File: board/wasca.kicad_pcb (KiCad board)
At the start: 2 copper layers, 64 parts, among them CN1 CARTRIDGE_EDGE_CONNECTOR, CON1 SD_Card, CON2 USB_OTG, CON3 Thermal_Quad, IC1 MT48LC32M16A2TG, U1 74ALVC164245, U2 74ALVC164245, U3 74ALVC164245, U4 74ALVC164245, U5 LD1117S33CTR, U6 10M04SFE144C8G, U7 FT201XS

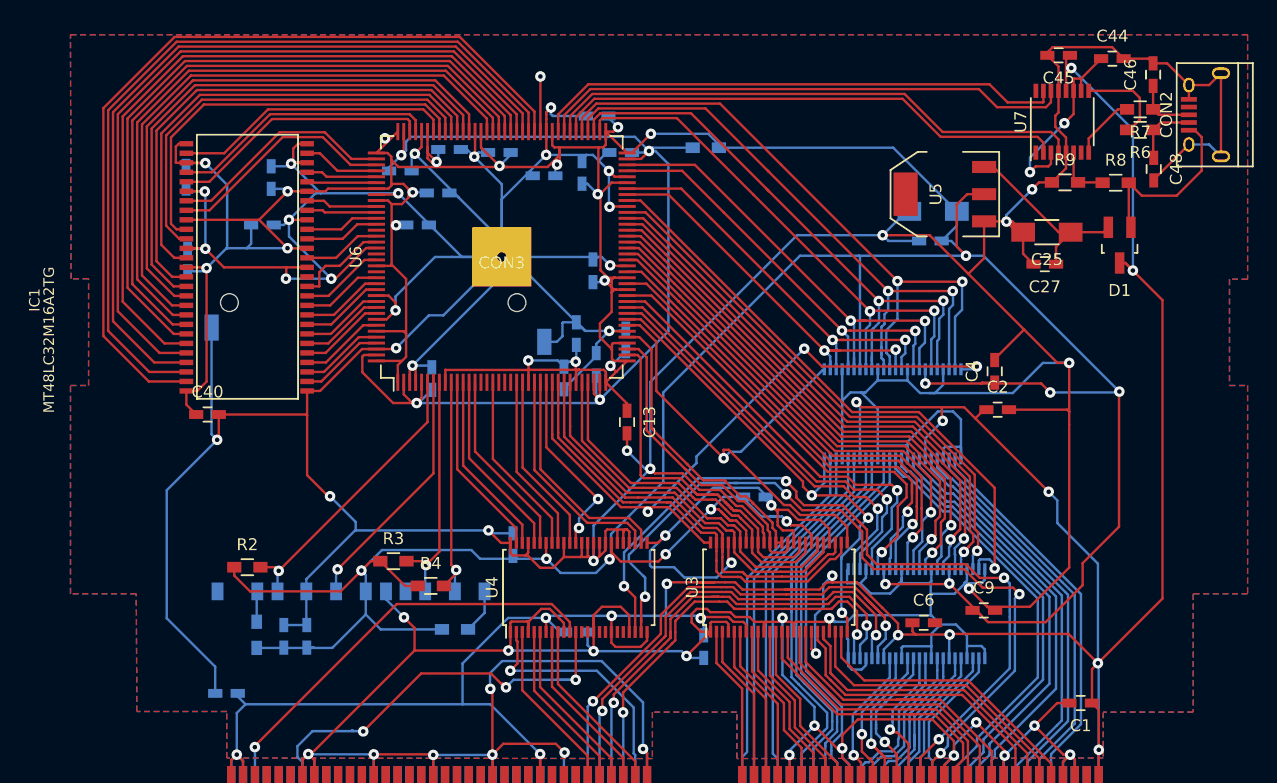
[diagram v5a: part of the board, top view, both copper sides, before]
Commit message: Silkscreen fix
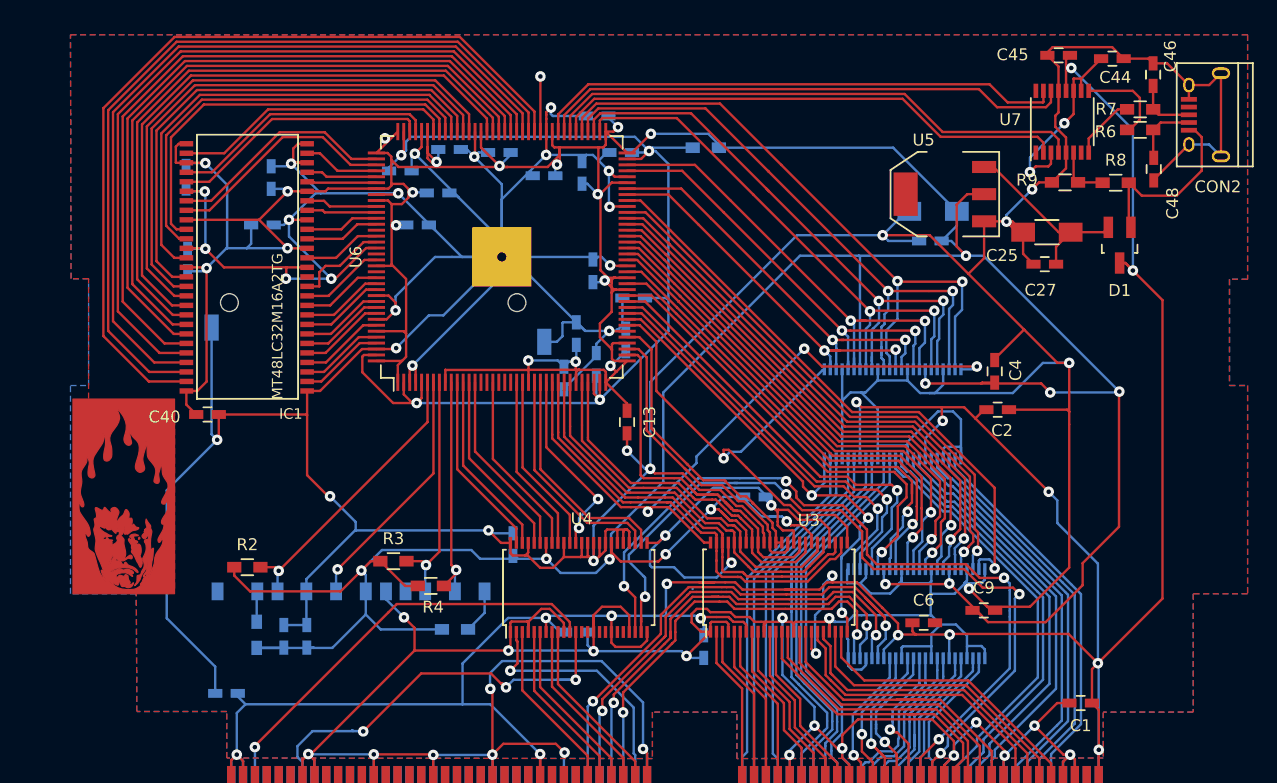
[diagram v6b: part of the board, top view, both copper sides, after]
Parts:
- added G***: LOGO, Wasca:Segata_Sanshiro, F.Cu at (31.8, 127.6)
- moved C28 18.3 mm to (74.7, 110.9), turned to 180 degrees
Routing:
- net /+3_3V: track 485.3 -> 487.6 mm
- net GND: track 972.5 -> 973.8 mm

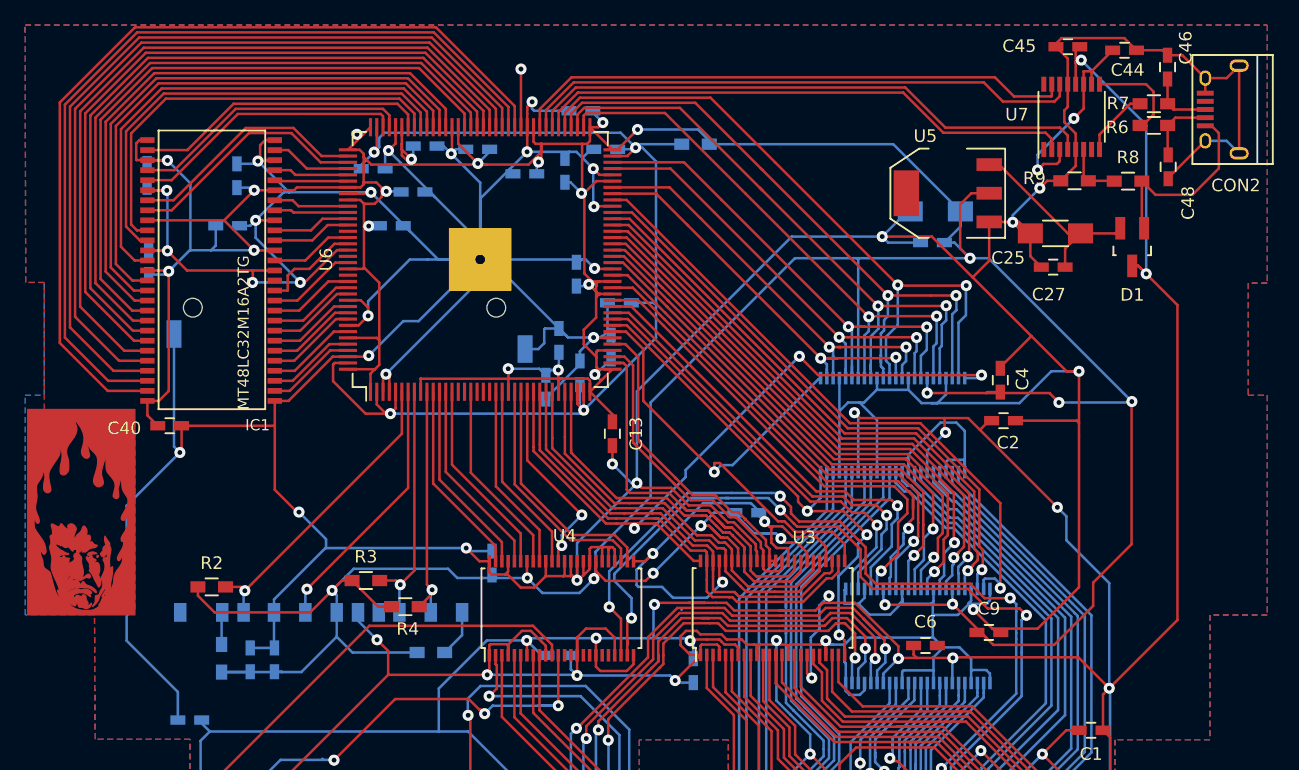
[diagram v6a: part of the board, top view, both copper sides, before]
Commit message: Board cleanup, intersected parts fix (thanks cafealpha2), more ground vias.
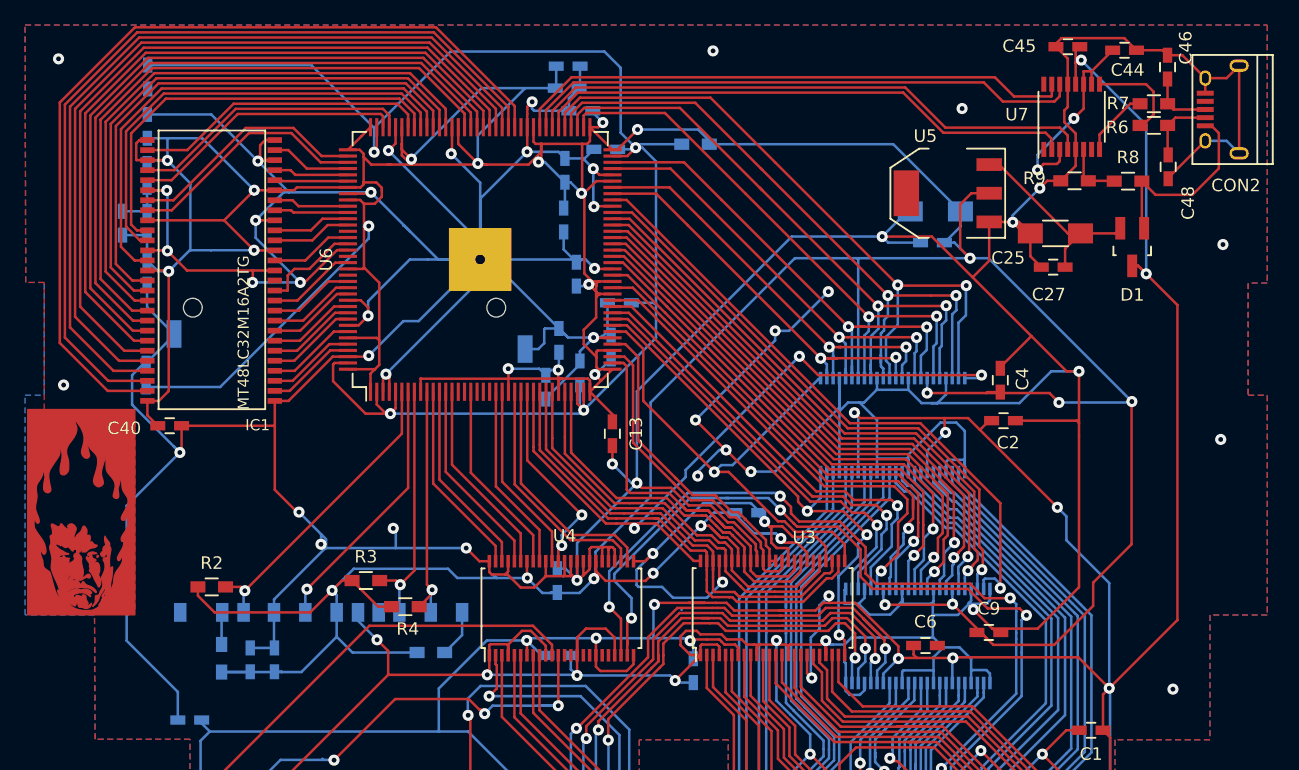
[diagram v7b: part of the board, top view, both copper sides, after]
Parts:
- moved C34 23.3 mm to (35.1, 104.5), turned to 90 degrees
- moved C35 22.9 mm to (37.0, 116.7), turned to 90 degrees
- moved C24 19.4 mm to (37.1, 92.9), turned to 270 degrees
- moved C37 13.1 mm to (70.6, 92.0)
- moved C32 8.64 mm to (70.6, 93.8), turned to 0 degrees
- moved C42 8.15 mm to (37.1, 96.8)
- moved C50 6.43 mm to (37.1, 104.5), turned to 90 degrees
- moved C10 5.39 mm to (69.8, 133.0)
- moved C36 4.81 mm to (70.3, 104.3), turned to 270 degrees
- moved C39 0.77 mm to (37.1, 108.5), turned to 270 degrees
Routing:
- net /+3_3V: track 487.6 -> 545.9 mm, vias 29 -> 27
- net GND: track 973.8 -> 1030.3 mm, vias 53 -> 61
- net Net-(C23-Pad1): track 93.3 -> 120.8 mm
- net Net-(U6-Pad84): track 4.64 -> 0.00 mm, vias 1 -> 0
- net /ABUS_3V_MUX_EN2: track 41.9 -> 40.9 mm
- net (no net): vias 0 -> 7

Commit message: Silkscreen cleanup
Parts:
- renumbered IC1 to U8
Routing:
- net GND: track 1030.3 -> 1147.1 mm, vias 61 -> 68
- net (no net): vias 7 -> 0
